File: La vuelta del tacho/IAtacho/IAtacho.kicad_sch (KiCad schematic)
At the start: 8 parts, among them J1 12V de la fuente regulable, J2 5v del step down, J3 motor paso a paso, J4 motor paso a paso, J6 ServoMotor

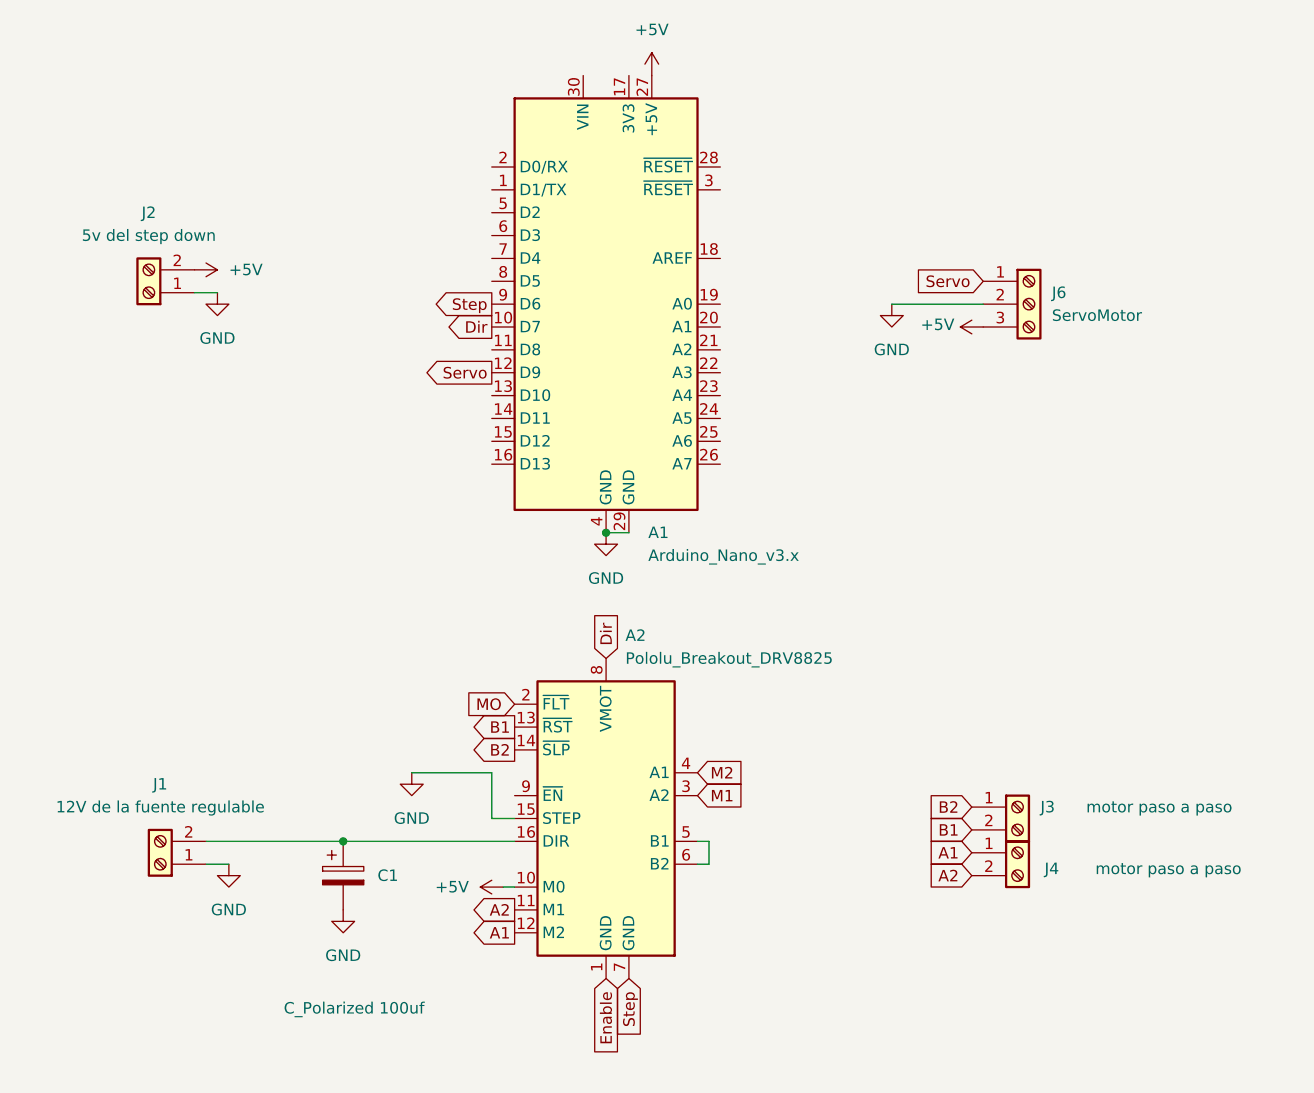
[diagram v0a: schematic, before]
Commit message: PCB arreglado sin 5v al arduino nano
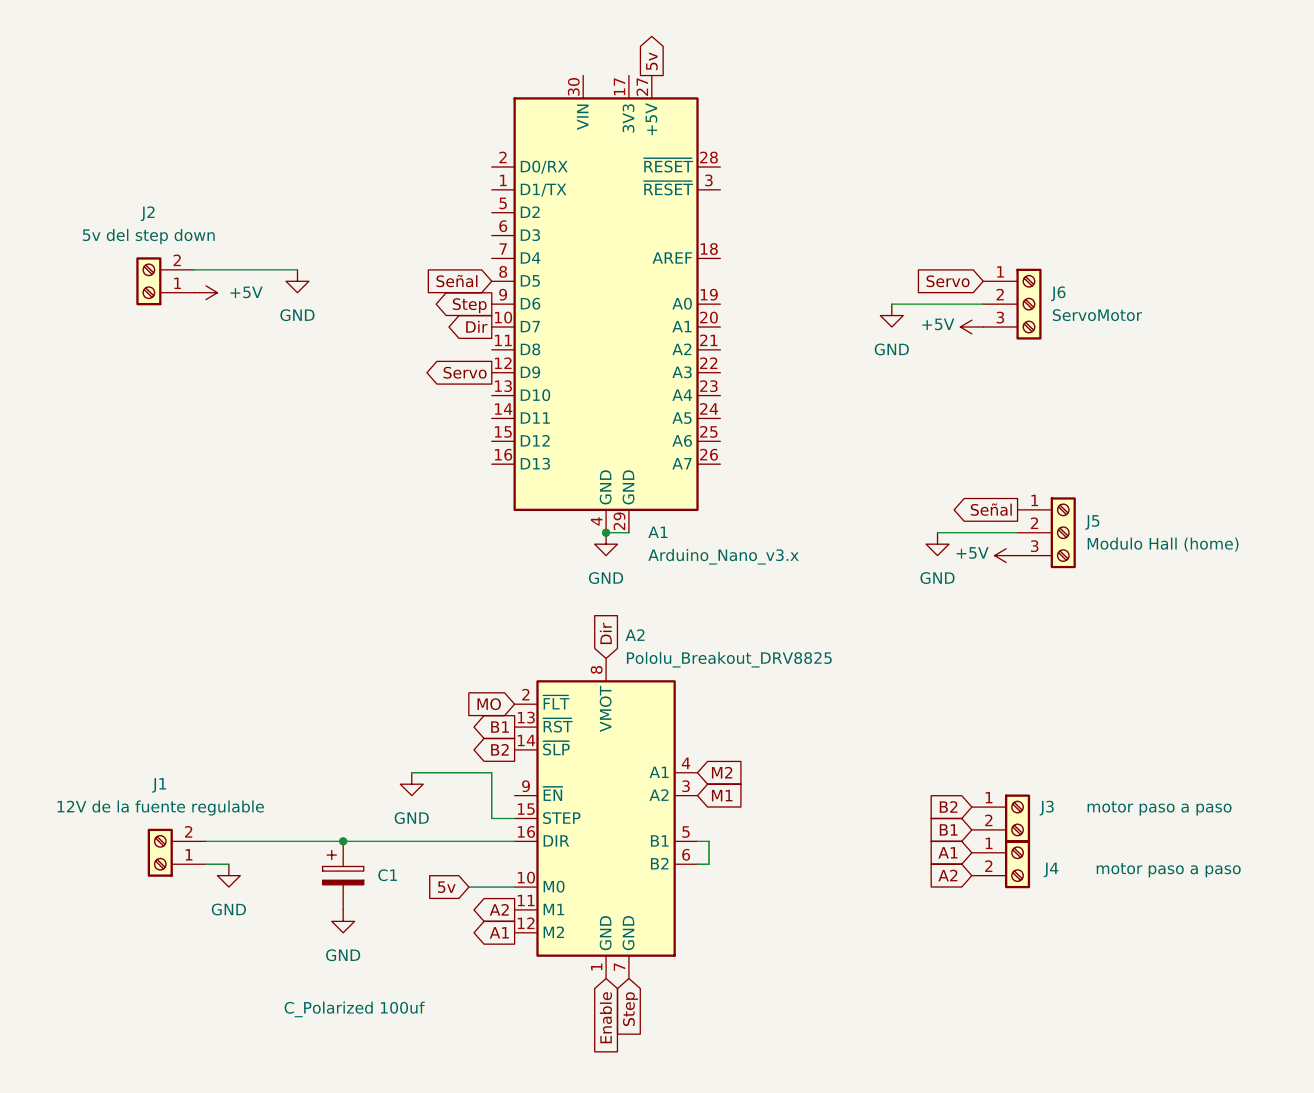
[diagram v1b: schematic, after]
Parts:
- added J5: Modulo Hall (home), TerminalBlock:TerminalBlock_MaiXu_MX126-5.0-03P_1x03_P5.00mm, symbol Connector:Screw_Terminal_01x03
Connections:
- net +5V: now also J2.1 (Pin_1), J5.3 (Pin_3); no longer A1.27 (+5V), A2.10 (M0), J2.2 (Pin_2)
- net GND: now also J2.2 (Pin_2), J5.2 (Pin_2); no longer J2.1 (Pin_1)
- net Señal : now reaches A1.8 (D5)
- net Señal : now also J5.1 (Pin_1)
- new net 5v: A1.27 (+5V), A2.10 (M0)
